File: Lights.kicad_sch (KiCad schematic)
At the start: 8 parts, among them U1 EL3H7, U6 EL3H7

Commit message: fixed some footprints and part numbers
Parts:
- R10, R5: Mouser Part Number (none) -> 71-CRCW08054K99FKEAC
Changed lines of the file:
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@@
+			)
+		)
+		(property "Mouser Part Number" "71-CRCW08054K99FKEAC "
+			(at 167.64 97.79 0)
+			(effects
+				(font
+					(size 1.27 1.27)
+				)
+				(hide yes)
 			)
 		)
@@
 			(at 168.91 138.43 0)
 			(effects
+				(font
+					(size 1.27 1.27)
+				)
+				(hide yes)
+			)
+		)
+		(property "Mouser Part Number" "71-CRCW08054K99FKEAC "
+			(at 168.91 138.43 0)
+			(effects

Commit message: Added/checked datasheet links/part numbers, deleted accel_pot2 and brake_pot2 hierarchical labels and changed corresponding pins (PC2, PC3) to GPIO on the now-2x5 extra GPIO connector.
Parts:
- R10, R5: Mouser Part Number 71-CRCW08054K99FKEAC -> 71-CRCW08052K00FKEC
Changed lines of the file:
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@@
 			)
 		)
-		(property "Datasheet" "https://everlightamericas.com/index.php?controller=attachment&id_attachment=2584"
+		(property "Datasheet" "https://www.mouser.com/ProductDetail/Everlight/EL3H7DTA-VG?qs=8PzhAHr7IdO5ivSzPAFioA%3D%3D&utm_id=21629221803&gad_source=1&gclid=Cj0KCQiArby5BhCDARIsAIJvjIRxO0jcjcKfnV1hER0ZGDMF9W_FecGmdKXwVqQCsmJYIZvEtRfuUkAaAnFwEALw_wcB"
 			(at 170.18 85.09 0)
 			(effects
@@
 			)
 		)
-		(property "Datasheet" "https://everlightamericas.com/index.php?controller=attachment&id_attachment=2584"
+		(property "Datasheet" "https://www.mouser.com/ProductDetail/Everlight/EL3H7DTA-VG?qs=8PzhAHr7IdO5ivSzPAFioA%3D%3D&utm_id=21629221803&gad_source=1&gclid=Cj0KCQiArby5BhCDARIsAIJvjIRxO0jcjcKfnV1hER0ZGDMF9W_FecGmdKXwVqQCsmJYIZvEtRfuUkAaAnFwEALw_wcB"
 			(at 171.45 125.73 0)
 			(effects
@@
 			)
 		)
-		(property "Datasheet" "~"
+		(property "Datasheet" "https://www.mouser.in/ProductDetail/Vishay-Dale/CRCW08052K00FKEC?qs=t8V6zXf%2FKwZmLP5kGUKwKw%3D%3D"
 			(at 167.64 97.79 0)
 			(effects
@@
 			)
 		)
-		(property "Mouser Part Number" "71-CRCW08054K99FKEAC "
+		(property "Mouser Part Number" "71-CRCW08052K00FKEC"
 			(at 167.64 97.79 0)
 			(effects
@@
 			)
 		)
-		(property "Datasheet" "~"
+		(property "Datasheet" "https://www.mouser.in/ProductDetail/Vishay-Dale/CRCW08052K00FKEC?qs=t8V6zXf%2FKwZmLP5kGUKwKw%3D%3D"
 			(at 168.91 138.43 0)
 			(effects
@@
 			)
 		)
-		(property "Mouser Part Number" "71-CRCW08054K99FKEAC "
+		(property "Mouser Part Number" "71-CRCW08052K00FKEC"
 			(at 168.91 138.43 0)
 			(effects

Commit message: Changed EL3H7 footprint from through-hole to SMD.
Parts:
- U1, U6: footprint Package_DIP:DIP-4_W7.62mm -> Package_SO:SSOP-4_4.4x2.6mm_P1.27mm
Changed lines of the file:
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@@
 			)
 		)
-		(property "Footprint" "Package_DIP:DIP-4_W7.62mm"
+		(property "Footprint" "Package_SO:SSOP-4_4.4x2.6mm_P1.27mm"
 			(at 175.26 90.17 0)
 			(effects
@@
 			)
 		)
-		(property "Footprint" "Package_DIP:DIP-4_W7.62mm"
+		(property "Footprint" "Package_SO:SSOP-4_4.4x2.6mm_P1.27mm"
 			(at 176.53 130.81 0)
 			(effects

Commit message: Moved some things inward and squished board, added some labels, broke some traces up (sorry Krish 😣)
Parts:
- TP7, TP8: footprint TestPoint:TestPoint_Pad_1.5x1.5mm -> TestPoint:TestPoint_Keystone_5005-5009_Compact
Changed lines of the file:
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@@
 			)
 		)
-		(property "Footprint" "TestPoint:TestPoint_Pad_1.5x1.5mm"
+		(property "Footprint" "TestPoint:TestPoint_Keystone_5005-5009_Compact"
 			(at 213.36 118.11 0)
 			(effects
@@
 			)
 		)
-		(property "Footprint" "TestPoint:TestPoint_Pad_1.5x1.5mm"
+		(property "Footprint" "TestPoint:TestPoint_Keystone_5005-5009_Compact"
 			(at 212.09 77.47 0)
 			(effects

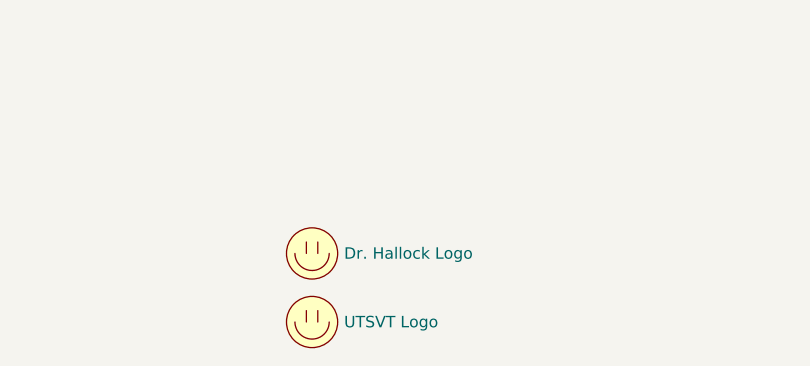
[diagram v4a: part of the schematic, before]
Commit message: Updated some symbols to use common libraries (and get rid of warnings.
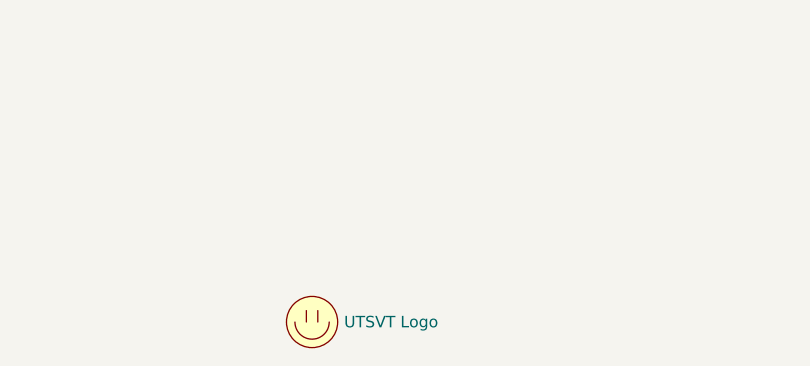
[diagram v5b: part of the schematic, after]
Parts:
- removed LOGO3: Dr. Hallock Logo, UTSVT_Special:Hallock_Image_Small, symbol Controls-LightingPCB-rescue:Logo_Placeholder-utsvt-misc
- LOGO4: symbol Controls-LightingPCB-rescue:Logo_Placeholder-utsvt-misc -> utsvt-misc:Logo_Placeholder
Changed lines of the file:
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@@
 	)
 	(symbol
-		(lib_id "Controls-LightingPCB-rescue:Logo_Placeholder-utsvt-misc")
+		(lib_id "utsvt-misc:Logo_Placeholder")
 		(at 128.905 189.23 0)
 		(unit 1)
@@
 					(unit 1)
 				)
-			)
-		)
-	)
-	(symbol
-		(lib_id "Controls-LightingPCB-rescue:Logo_Placeholder-utsvt-misc")
-		(at 128.905 181.61 0)
-		(unit 1)
-		(exclude_from_sim no)
-		(in_bom yes)
-		(on_board yes)
-		(dnp no)
-		(property "Reference" "LOGO3"
-			(at 128.905 177.8 0)
-			(effects
-				(font
-					(size 1.27 1.27)
-				)
-				(hide yes)
-			)
-		)
-		(property "Value" "Dr. Hallock Logo"
-			(at 132.461 181.61 0)
-			(effects
-				(font
-					(size 1.27 1.27)
-				)
-				(justify left)
-			)
-		)
-		(property "Footprint" "UTSVT_Special:Hallock_Image_Small"
-			(at 128.905 179.705 0)
-			(effects
-				(font
-					(size 1.27 1.27)
-				)
-				(hide yes)
-			)
-		)
-		(property "Datasheet" ""
-			(at 128.905 179.705 0)
-			(effects
-				(font
-					(size 1.27 1.27)
-				)
-				(hide yes)
-			)
-		)
-		(property "Description" ""
-			(at 128.905 181.61 0)
-			(effects
-				(font
-					(size 1.27 1.27)
-				)
-				(hide yes)
-			)
-		)
-		(property "Id" ""
-			(at 128.905 181.61 0)
-			(effects
-				(font
-					(size 1.27 1.27)
-				)
-				(hide yes)
-			)
-		)
-		(property "Vds" ""
-			(at 128.905 181.61 0)
-			(effects
-				(font
-					(size 1.27 1.27)
-				)
-				(hide yes)
-			)
-		)
-		(instances
-			(project "Controls-Leader"
-				(path "/66218487-e316-4467-9eba-79d4626ab24e/c2b44a2f-ee1f-4a43-89f7-eda540df1696"
-					(reference "LOGO3")
-					(unit 1)
-				)

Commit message: Filled in part numbers, exported BOM and made Excel file for working with it.
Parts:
- R10, R5: P/N (none) -> CRCW08052K00FKEC
- U1, U6: P/N (none) -> EL3H7DTAVG
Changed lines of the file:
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@@
+			)
+		)
+		(property "P/N" "EL3H7DTAVG "
+			(at 170.18 85.09 0)
+			(effects
+				(font
+					(size 1.27 1.27)
+				)
+				(hide yes)
 			)
 		)
@@
 			)
 		)
+		(property "P/N" "EL3H7DTAVG "
+			(at 171.45 125.73 0)
+			(effects
+				(font
+					(size 1.27 1.27)
+				)
+				(hide yes)
+			)
+		)
 		(pin "1"
 		)
@@
 			)
 		)
+		(property "P/N" "CRCW08052K00FKEC"
+			(at 167.64 97.79 0)
+			(effects
+				(font
+					(size 1.27 1.27)
+				)
+				(hide yes)
+			)
+		)
 		(pin "2"
 		)
@@
 			(at 168.91 138.43 0)
 			(effects
+				(font
+					(size 1.27 1.27)
+				)
+				(hide yes)
+			)
+		)
+		(property "P/N" "CRCW08052K00FKEC"
+			(at 168.91 138.43 0)
+			(effects

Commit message: Added version update notes.
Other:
- note added: "- Replaced lights drivers/circuits - Replaced 555 timer with blinking gpio that passes through to drivers when dashboard Left/Right 3-pos switch is toggled - Intended to connect to breakout boards that split out the necessary number of lights"
- note removed: "Version History"
- note removed: "v1.0 - Created Lighting Board with outputs to all external & internal lights - All buttons/switches on driver dashboard are debounced and sent to Control Leader Board v1.1 - Added opto-isolators to external lights output - Change TVS diode to be SMD - Changed reverse polarity protection to MOSFET instead of diode"
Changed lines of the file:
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@@
 		)
 	)
-	(rectangle
-		(start 203.835 23.749)
-		(end 278.13 44.45)
-		(stroke
-			(width 0)
-			(type default)
-		)
-		(fill
-			(type none)
-		)
-	)
-	(text "Version History"
+	(text "- Replaced lights drivers/circuits\n- Replaced 555 timer with blinking gpio \n   that passes through to drivers when dashboard Left/Right 3-pos switch is toggled\n- Intended to connect to breakout boards that split out the necessary number of lights"
 		(exclude_from_sim no)
-		(at 204.47 27.94 0)
+		(at 178.054 180.34 0)
 		(effects
 			(font
-				(size 2 2)
-				(thickness 1)
-				(bold yes)
+				(face "KiCad Font")
+				(size 1.524 1.524)
+				(thickness 0.1905)
+				(color 255 2 13 1)
 			)
 			(justify left bottom)
-		)
-	)
-	(text "v1.0\n- Created Lighting Board with outputs to all external & internal lights\n- All buttons/switches on driver dashboard are debounced and sent to Control Leader Board\n\nv1.1\n- Added opto-isolators to external lights output\n- Change TVS diode to be SMD\n- Changed reverse polarity protection to MOSFET instead of diode\n\n"
-		(exclude_from_sim no)
-		(at 205.74 43.18 0)
-		(effects
-			(font
-				(size 1 1)
-			)
-			(justify left bottom)

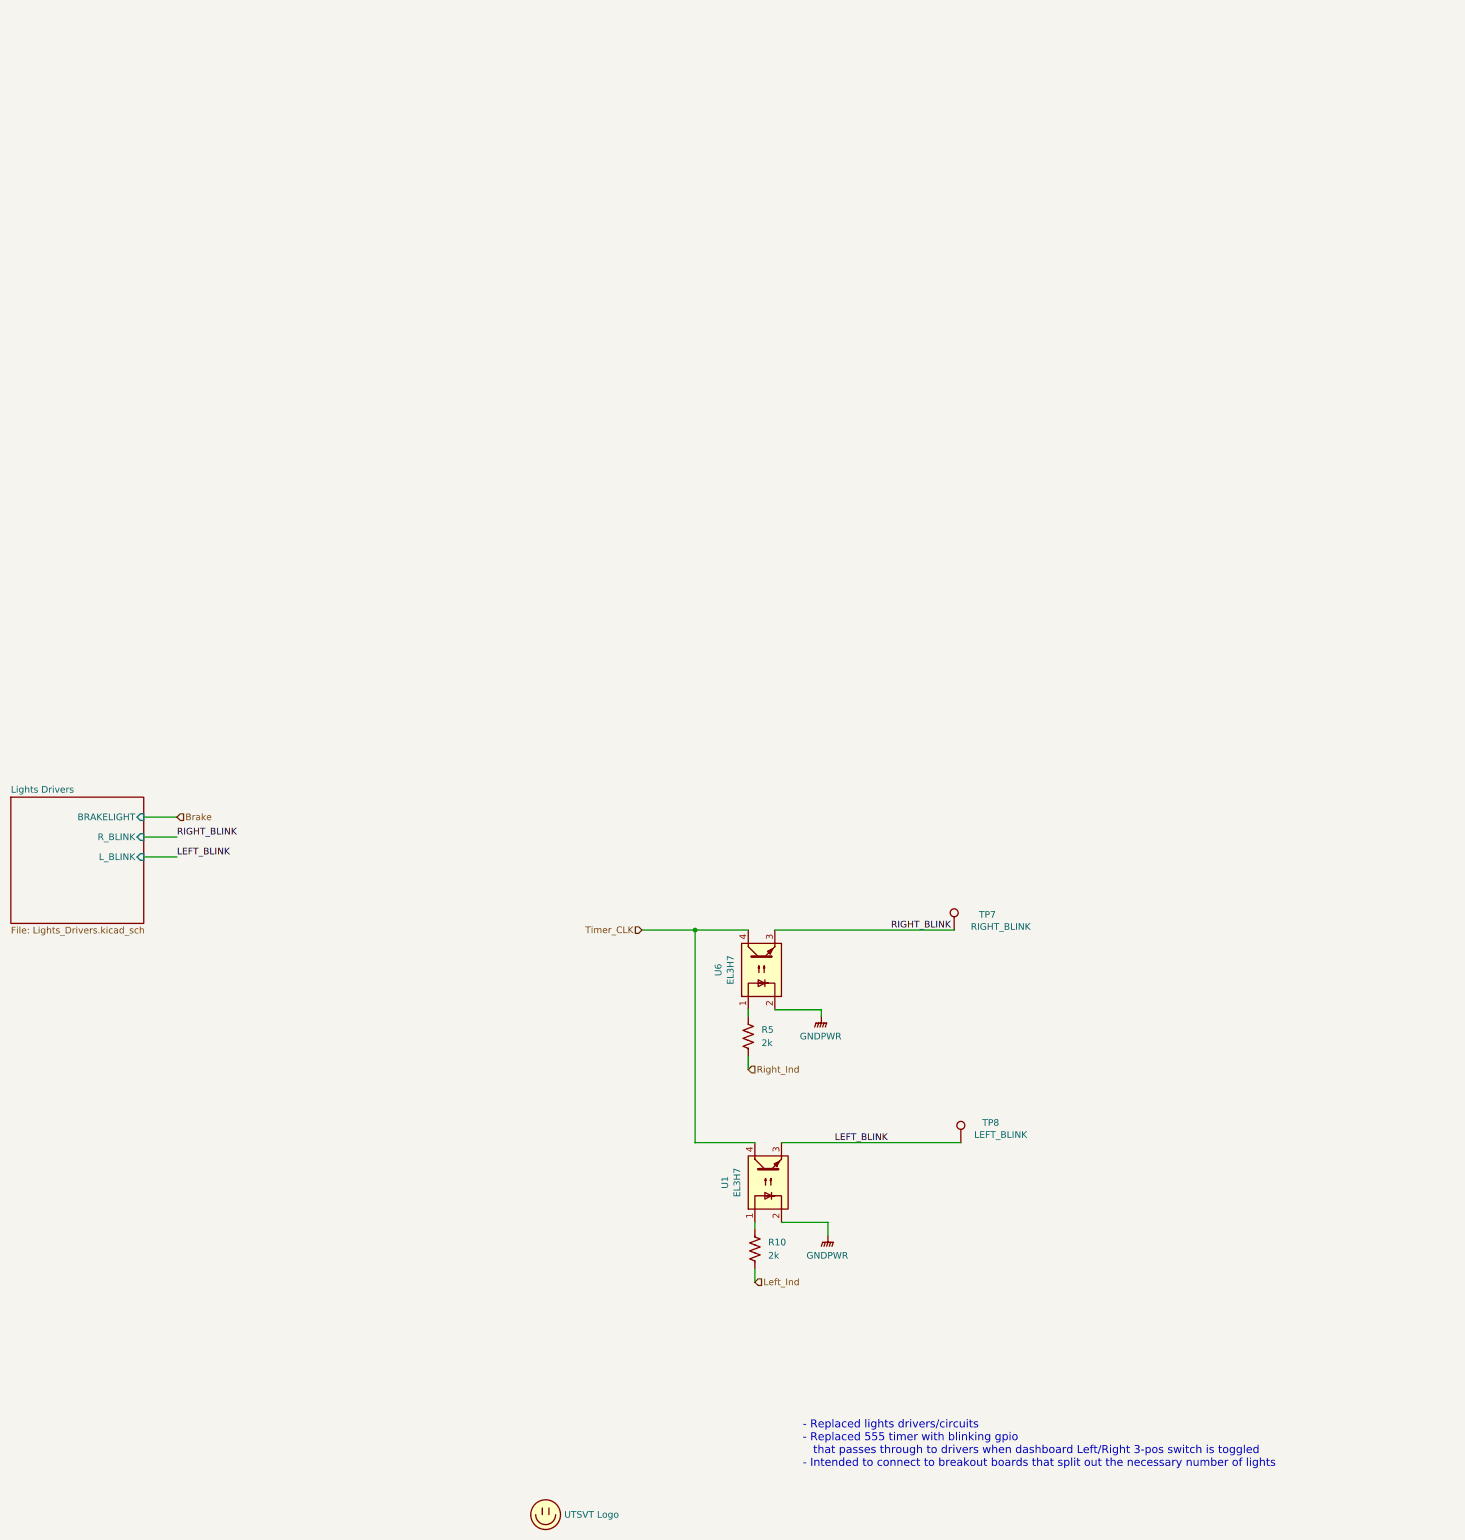
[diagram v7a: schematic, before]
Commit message: Changed lights to direct drive instead of timer_CLK optoisolator stuff.
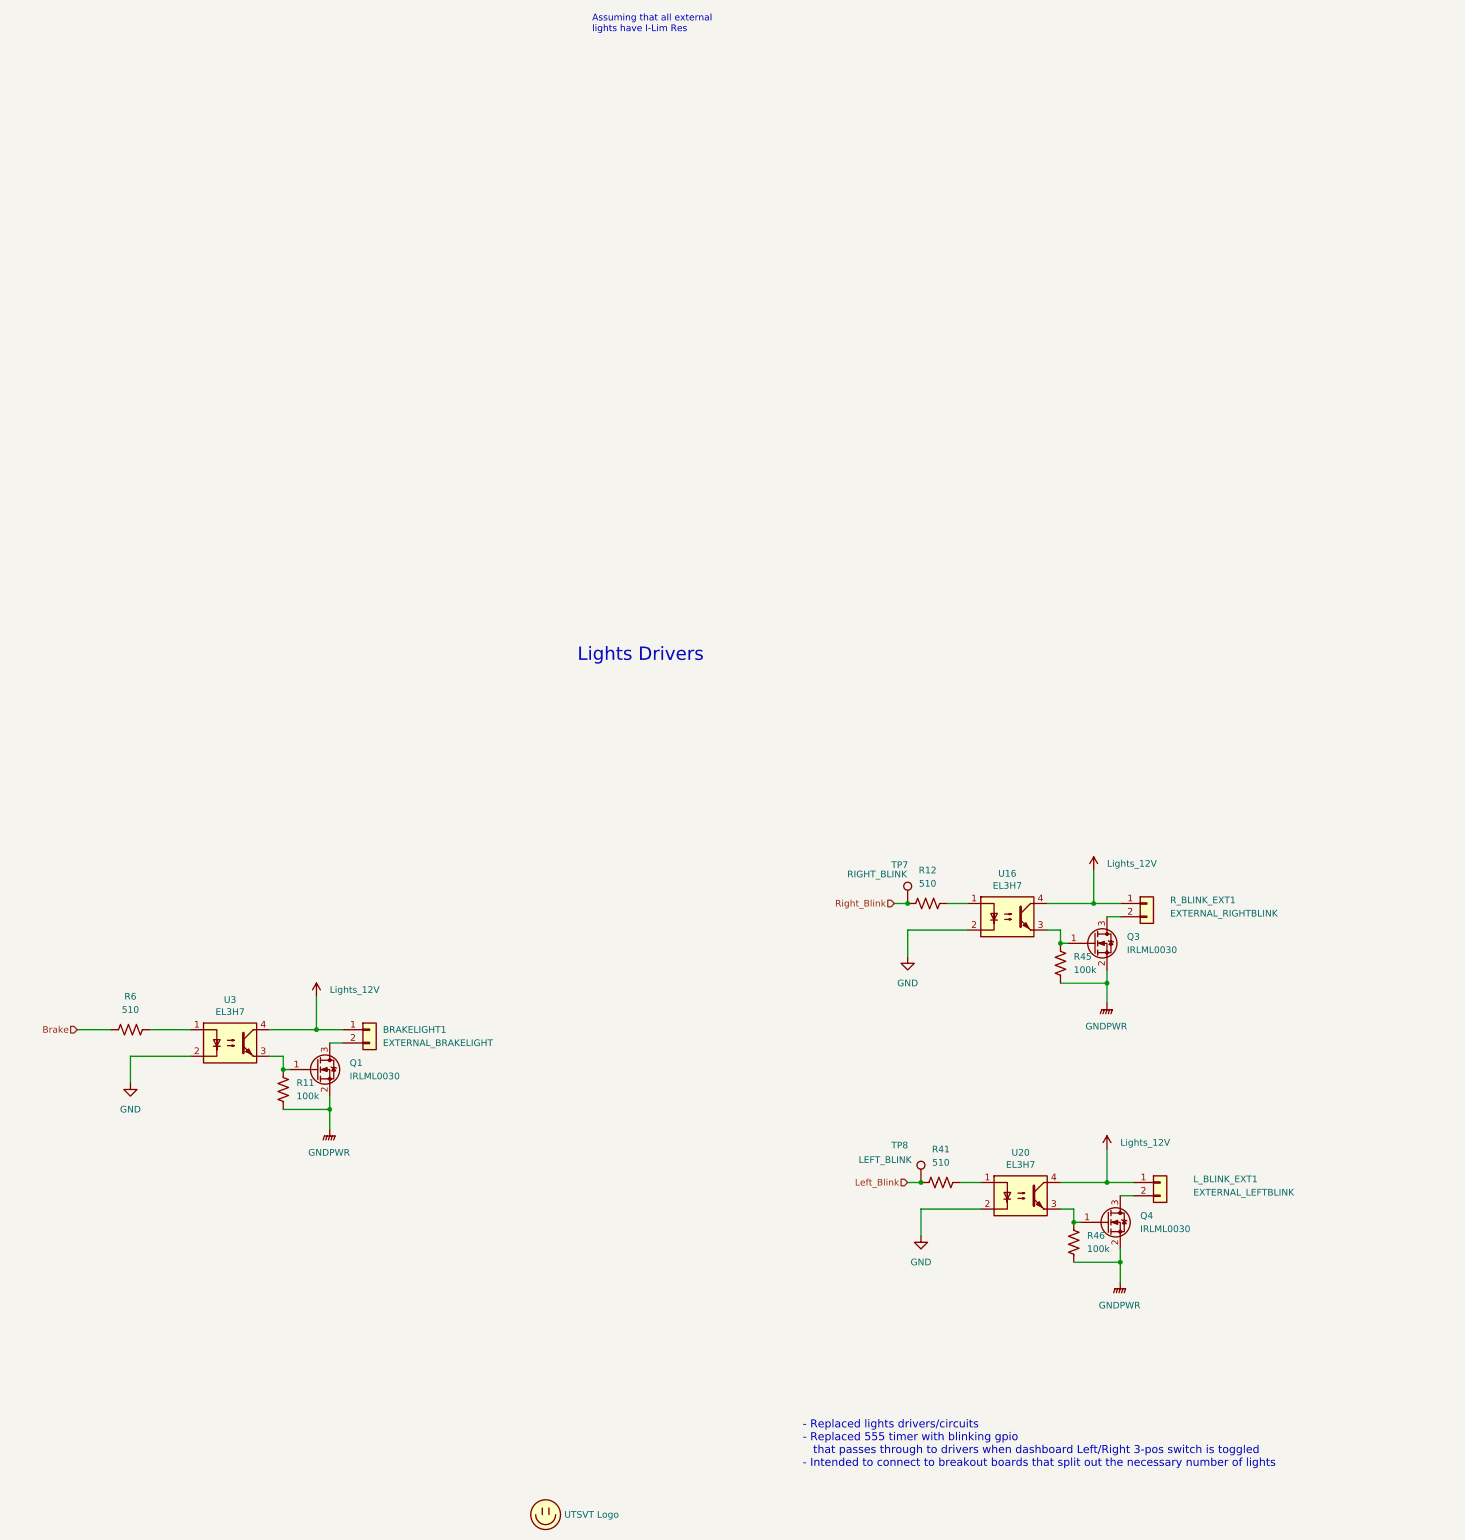
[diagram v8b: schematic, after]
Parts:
- removed R10, R5: 2k, Resistor_SMD:R_0805_2012Metric, symbol Device:R_US
- removed U1, U6: EL3H7, Package_SO:SSOP-4_4.4x2.6mm_P1.27mm, symbol Isolator:SFH617A-1
- added BRAKELIGHT1: EXTERNAL_BRAKELIGHT, Connector_Molex:Molex_Micro-Fit_3.0_43650-0215_1x02_P3.00mm_Vertical, symbol Connector_Generic:Conn_01x02
- added L_BLINK_EXT1: EXTERNAL_LEFTBLINK, Connector_Molex:Molex_Micro-Fit_3.0_43650-0215_1x02_P3.00mm_Vertical, symbol Connector_Generic:Conn_01x02
- added Q1, Q3, Q4: IRLML0030, Package_TO_SOT_SMD:SOT-23, symbol Transistor_FET:IRLML0030
- added R11, R45, R46: 100k, Resistor_SMD:R_0805_2012Metric, symbol Device:R_US
- added R12, R41, R6: 510, Resistor_SMD:R_0805_2012Metric, symbol Device:R_US
- added R_BLINK_EXT1: EXTERNAL_RIGHTBLINK, Connector_Molex:Molex_Micro-Fit_3.0_43650-0215_1x02_P3.00mm_Vertical, symbol Connector_Generic:Conn_01x02
- added U16, U20, U3: EL3H7, Package_SO:SSOP-4_4.4x2.6mm_P1.27mm, symbol Isolator:SFH617A-1
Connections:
- net Brake: now also R6.1
- net GNDPWR: now also Q1.2 (S), Q3.2 (S), Q4.2 (S), R11.2, R45.2, R46.2
- net LEFT_BLINK renamed Left_Blink
- net Left_Blink: now also R41.1
- net RIGHT_BLINK renamed Right_Blink
- net Right_Blink: now also R12.1
- new net: Q3.3 (D), R_BLINK_EXT1.2 (Pin_2)
- new net: Q1.1 (G), R11.1, U3.3
- new net: Q3.1 (G), R45.1, U16.3
- new net: L_BLINK_EXT1.2 (Pin_2), Q4.3 (D)
- new net: BRAKELIGHT1.2 (Pin_2), Q1.3 (D)
- new net: R12.2, U16.1
- new net: Q4.1 (G), R46.1, U20.3
- new net: R41.2, U20.1
- new net: R6.2, U3.1
- new net GND: U16.2, U20.2, U3.2
- new net Lights_12V: BRAKELIGHT1.1 (Pin_1), L_BLINK_EXT1.1 (Pin_1), R_BLINK_EXT1.1 (Pin_1), U16.4, U20.4, U3.4
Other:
- removed sheet Lights Drivers
- note added: "Assuming that all external lights have I-Lim Res"
- note added: "Lights Drivers"
- moved on the sheet: TP7, TP8
